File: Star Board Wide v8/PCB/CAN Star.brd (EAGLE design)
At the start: 124.7 x 37.3 mm, 24 parts

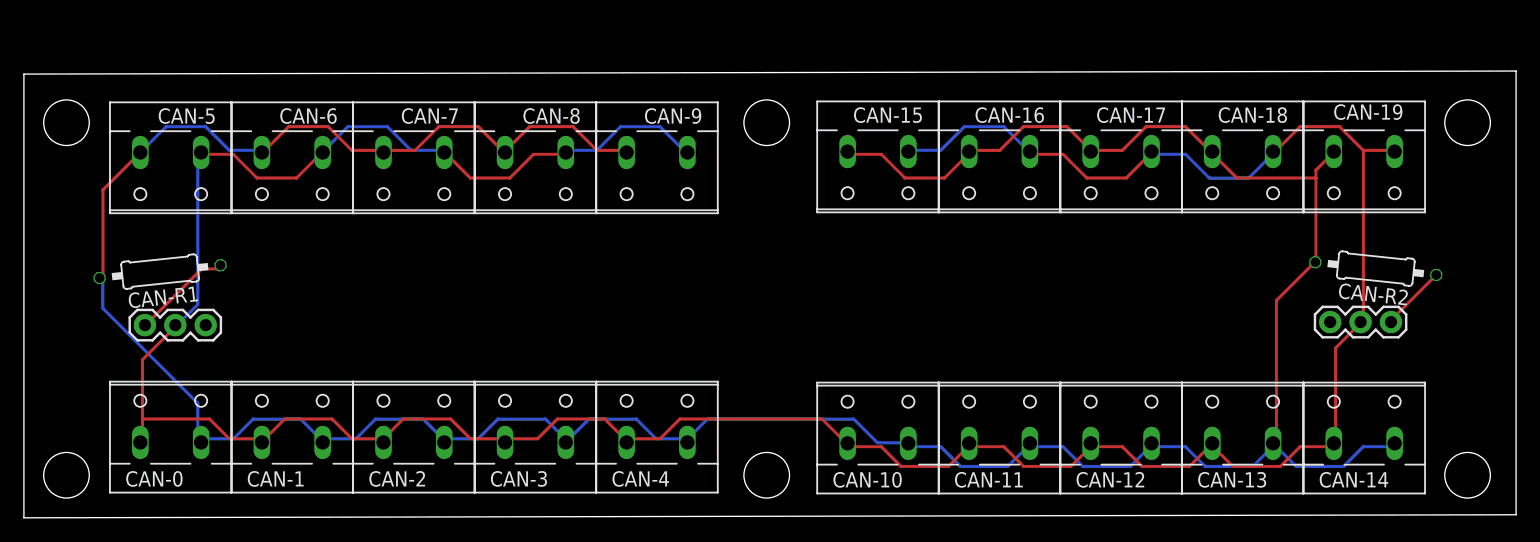
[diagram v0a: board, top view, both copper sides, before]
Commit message: switch to wide-v9, add in grounds, removed odd connections, needs layout work
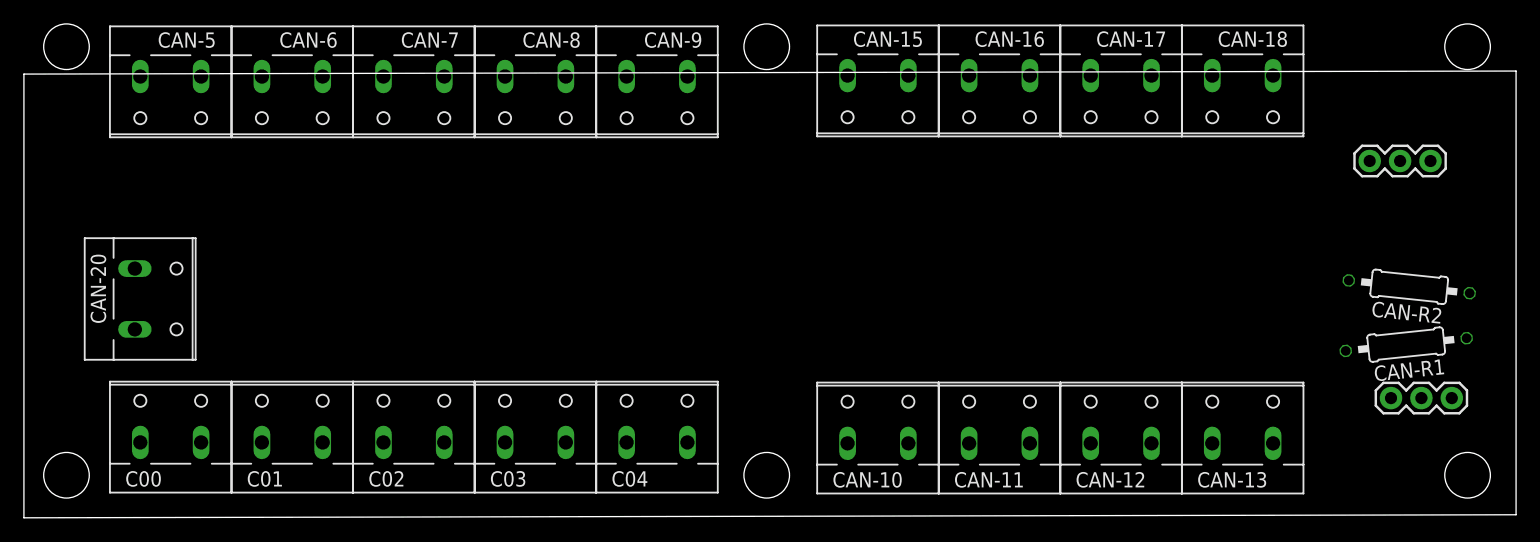
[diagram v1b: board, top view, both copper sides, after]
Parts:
- removed CAN-14: CAN 4, con-wago-508:W237-132
- removed CAN-19: CAN 9, con-wago-508:W237-132
- added CAN-20: CAN GND, con-wago-508:W237-132
- C00: value CAN 0 -> (none)
- moved CAN-R1 104.3 mm to (115.5, 14.5)
- moved JUMPER1 104.3 mm to (114.3, 10.0)
- moved JUMPER2 13.9 mm to (117.5, 29.8)
- moved CAN-15 6.35 mm to (71.4, 36.3)
- moved CAN-16 6.35 mm to (81.5, 36.3)
- moved CAN-17 6.35 mm to (91.7, 36.3)
- moved CAN-18 6.35 mm to (101.9, 36.3)
- moved CAN-5 6.35 mm to (12.3, 36.2)
- moved CAN-6 6.35 mm to (22.4, 36.2)
- moved CAN-7 6.35 mm to (32.6, 36.2)
- moved CAN-8 6.35 mm to (42.7, 36.2)
- moved CAN-9 6.35 mm to (52.9, 36.2)
- moved CAN-R2 3.18 mm to (115.8, 19.3)
- renumbered CAN-0 to C00, CAN-1 to C01, CAN-2 to C02, CAN-3 to C03, CAN-4 to C04
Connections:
- removed net CAN-A: C00.1, C01.1, C02.1, C03.1, C04.1, CAN-10.1, CAN-11.1, CAN-12.1, CAN-13.1, CAN-14.1, CAN-15.1, CAN-16.1, CAN-17.1, CAN-18.1, CAN-19.1, CAN-5.1, CAN-6.1, CAN-7.1, CAN-8.1, CAN-9.1, JUMPER1.2, JUMPER2.2
- removed net CAN-B: C00.2, C01.2, C02.2, C03.2, C04.2, CAN-10.2, CAN-11.2, CAN-12.2, CAN-13.2, CAN-14.2, CAN-15.2, CAN-16.2, CAN-17.2, CAN-18.2, CAN-19.2, CAN-5.2, CAN-6.2, CAN-7.2, CAN-8.2, CAN-9.2, CAN-R1.2, CAN-R2.2
- new net G: C00.2, C02.1, C03.2, CAN-10.1, CAN-11.2, CAN-13.1, CAN-15.2, CAN-16.1, CAN-18.2, CAN-5.1, CAN-7.2, CAN-8.1, CAN-R1.2, CAN-R2.2
- new net GND: C01.1, C02.2, C04.1, CAN-10.2, CAN-12.1, CAN-13.2, CAN-15.1, CAN-17.2, CAN-18.1, CAN-20.1, CAN-20.2, CAN-6.2, CAN-7.1, CAN-9.2
- new net Y: C00.1, C01.2, C03.1, C04.2, CAN-11.1, CAN-12.2, CAN-16.2, CAN-17.1, CAN-5.2, CAN-6.1, CAN-8.2, CAN-9.1, JUMPER1.2, JUMPER2.2
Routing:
- net CAN-B: track 264.5 -> 0.00 mm
- net CAN-A: track 261.7 -> 0.00 mm
- net N$1: track 8.40 -> 0.54 mm
- net N$2: track 5.50 -> 0.22 mm
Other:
- board text added: "GND"
- board text added: "Star Board Wide v9"
- board text removed: "Star Board Wide v8"

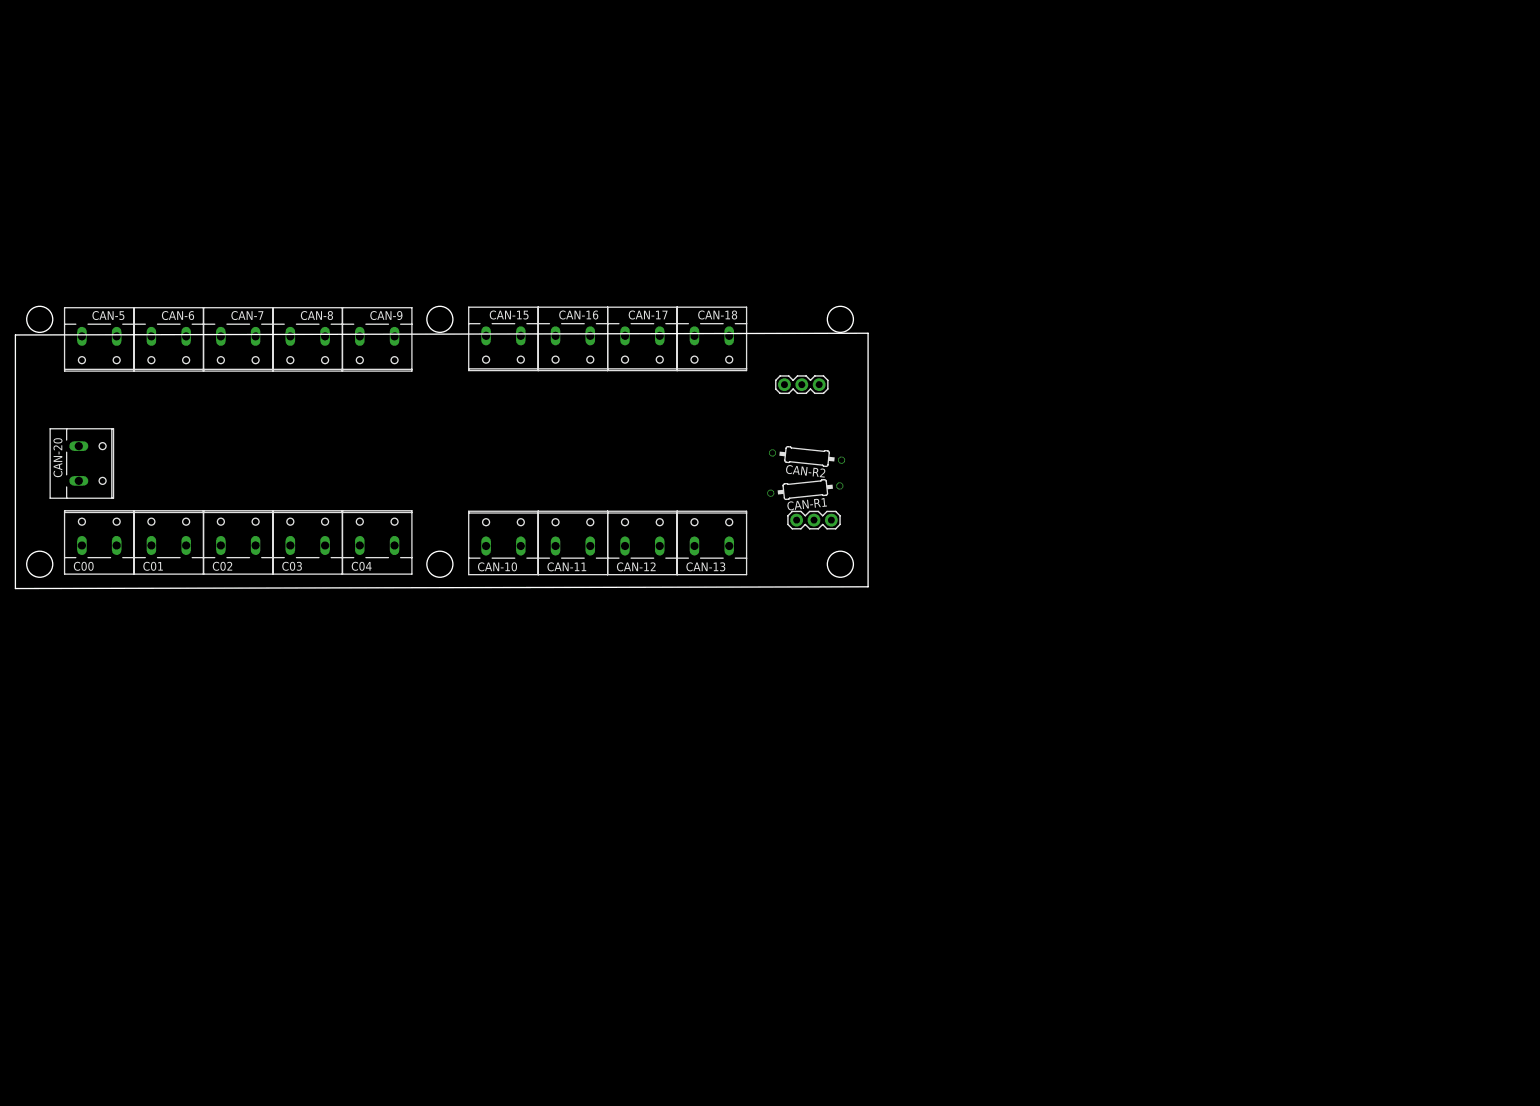
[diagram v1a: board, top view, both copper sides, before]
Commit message: change layout to 3 by 4
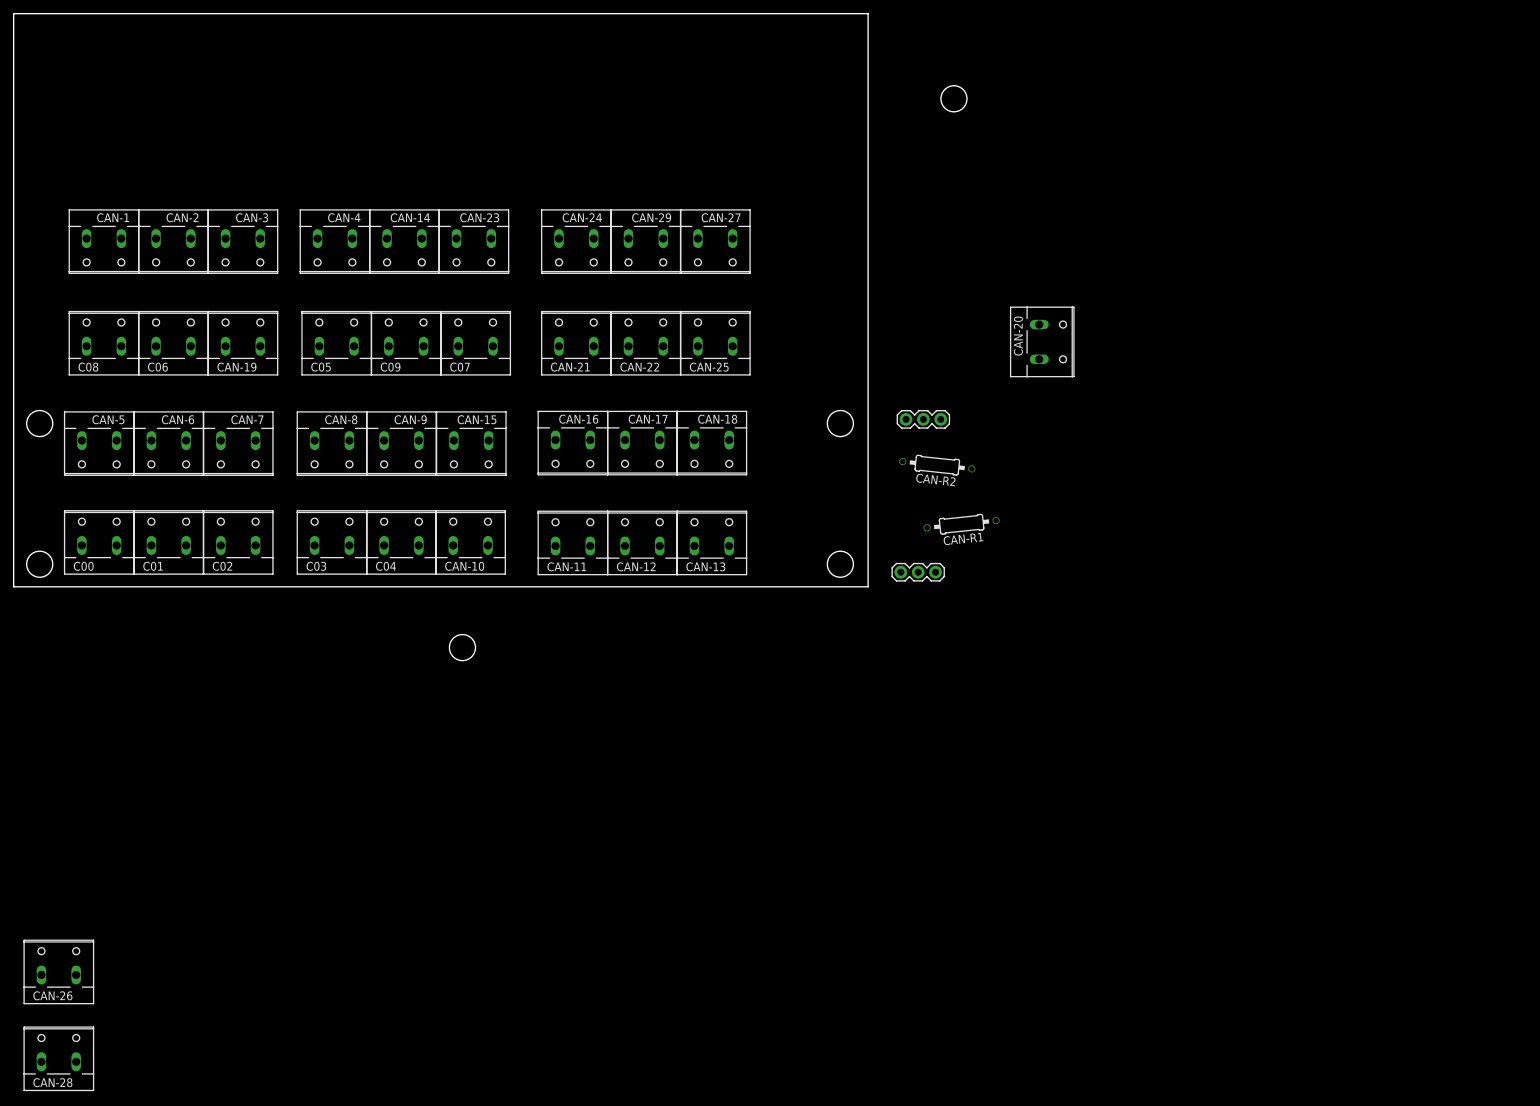
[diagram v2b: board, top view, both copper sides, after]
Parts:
- added C05: (no value), con-wago-508:W237-132
- added C06, CAN-21, CAN-26: CAN 1, con-wago-508:W237-132
- added C07, CAN-22, CAN-27: CAN 2, con-wago-508:W237-132
- added C08: CAN 3, con-wago-508:W237-132
- added C09: CAN 4, con-wago-508:W237-132
- added CAN-1, CAN-23: CAN 5, con-wago-508:W237-132
- added CAN-14: CAN 9, con-wago-508:W237-132
- added CAN-19: CAN 0, con-wago-508:W237-132
- added CAN-2, CAN-24, CAN-28: CAN 6, con-wago-508:W237-132
- added CAN-25, CAN-29, CAN-3: CAN 7, con-wago-508:W237-132
- added CAN-4: CAN 8, con-wago-508:W237-132
- moved CAN-20 141.6 mm to (150.4, 36.1)
- moved CAN-R1 23.4 mm to (138.4, 9.40)
- moved CAN-R2 19.1 mm to (134.8, 18.0)
- moved JUMPER2 18.5 mm to (135.3, 24.7)
- moved JUMPER1 17.0 mm to (129.5, 2.39)
- moved CAN-15 16.0 mm to (66.7, 21.0)
- moved CAN-8 15.6 mm to (46.3, 21.0)
- moved CAN-9 15.6 mm to (56.5, 21.0)
- moved CAN-16 15.2 mm to (81.5, 21.1)
- moved CAN-17 15.2 mm to (91.7, 21.1)
- moved CAN-18 15.2 mm to (101.9, 21.1)
- moved CAN-5 15.2 mm to (12.3, 21.0)
- moved CAN-6 15.2 mm to (22.4, 21.0)
- moved CAN-7 15.2 mm to (32.6, 21.0)
- moved CAN-10 4.80 mm to (66.6, 6.93)
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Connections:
- net G: now also C05.2, C07.1, C08.2, CAN-1.1, CAN-19.1, CAN-21.2, CAN-23.2, CAN-24.1, CAN-25.1, CAN-26.2, CAN-27.2, CAN-28.1, CAN-3.2, CAN-4.1
- net GND: now also C06.1, C07.2, C09.1, CAN-14.2, CAN-19.2, CAN-2.2, CAN-22.1, CAN-23.1, CAN-25.2, CAN-27.1, CAN-29.2, CAN-3.1
- net Y: now also C05.1, C06.2, C08.1, C09.2, CAN-1.2, CAN-14.1, CAN-2.1, CAN-21.1, CAN-22.2, CAN-24.2, CAN-26.1, CAN-28.2, CAN-29.1, CAN-4.2
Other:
- board size 124.7 x 37.3 mm -> 125 x 83.8 mm

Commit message: Remade board wide v9
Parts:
- removed C00, C05: (no value), con-wago-508:W237-132
- removed C01, C06, CAN-11, CAN-21, CAN-26: CAN 1, con-wago-508:W237-132
- removed C02, C07, CAN-12, CAN-22, CAN-27: CAN 2, con-wago-508:W237-132
- removed C03, C08, CAN-13: CAN 3, con-wago-508:W237-132
- removed C04, C09: CAN 4, con-wago-508:W237-132
- removed CAN-1, CAN-15, CAN-23, CAN-5: CAN 5, con-wago-508:W237-132
- removed CAN-10, CAN-19: CAN 0, con-wago-508:W237-132
- removed CAN-14, CAN-9: CAN 9, con-wago-508:W237-132
- removed CAN-16, CAN-2, CAN-24, CAN-28, CAN-6: CAN 6, con-wago-508:W237-132
- removed CAN-17, CAN-25, CAN-29, CAN-3, CAN-7: CAN 7, con-wago-508:W237-132
- removed CAN-18, CAN-4, CAN-8: CAN 8, con-wago-508:W237-132
- removed CAN-20: CAN GND, con-wago-508:W237-132
- removed CAN-R1, CAN-R2: 120Ω, resistor:0207/10
- removed JUMPER1, JUMPER2: (no value), SparkFun-Connectors:1X03
- added U$1, U$10, U$11, U$12, U$2, U$3, U$4, U$5, U$6, U$7, U$8, U$9: 2-3-TERMS, custom:GREEN-2-TERMS
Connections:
- removed net G: C00.2, C02.1, C03.2, C05.2, C07.1, C08.2, CAN-1.1, CAN-10.1, CAN-11.2, CAN-13.1, CAN-15.2, CAN-16.1, CAN-18.2, CAN-19.1, CAN-21.2, CAN-23.2, CAN-24.1, CAN-25.1, CAN-26.2, CAN-27.2, CAN-28.1, CAN-3.2, CAN-4.1, CAN-5.1, CAN-7.2, CAN-8.1, CAN-R1.2, CAN-R2.2
- removed net N$1: CAN-R1.1, JUMPER1.1
- removed net N$2: CAN-R2.1, JUMPER2.1
- removed net Y: C00.1, C01.2, C03.1, C04.2, C05.1, C06.2, C08.1, C09.2, CAN-1.2, CAN-11.1, CAN-12.2, CAN-14.1, CAN-16.2, CAN-17.1, CAN-2.1, CAN-21.1, CAN-22.2, CAN-24.2, CAN-26.1, CAN-28.2, CAN-29.1, CAN-4.2, CAN-5.2, CAN-6.1, CAN-8.2, CAN-9.1, JUMPER1.2, JUMPER2.2
- new net G(L): U$1.L0, U$1.L1, U$10.L0, U$10.L1, U$11.L0, U$11.L1, U$12.L0, U$12.L1, U$2.L0, U$2.L1, U$3.L0, U$3.L1, U$4.L0, U$4.L1, U$5.L0, U$5.L1, U$6.L0, U$6.L1, U$7.L0, U$7.L1, U$8.L0, U$8.L1, U$9.L0, U$9.L1
- new net Y(H): U$1.H0, U$1.H1, U$10.H0, U$10.H1, U$11.H0, U$11.H1, U$12.H0, U$12.H1, U$2.H0, U$2.H1, U$3.H0, U$3.H1, U$4.H0, U$4.H1, U$5.H0, U$5.H1, U$6.H0, U$6.H1, U$7.H0, U$7.H1, U$8.H0, U$8.H1, U$9.H0, U$9.H1
- net GND: now also U$1.GND0, U$1.GND1, U$10.GND0, U$10.GND1, U$11.GND0, U$11.GND1, U$12.GND0, U$12.GND1, U$2.GND0, U$2.GND1, U$3.GND0, U$3.GND1, U$4.GND0, U$4.GND1, U$5.GND0, U$5.GND1, U$6.GND0, U$6.GND1, U$7.GND0, U$7.GND1, U$8.GND0, U$8.GND1, U$9.GND0, U$9.GND1; no longer C01.1, C02.2, C04.1, C06.1, C07.2, C09.1, CAN-10.2, CAN-12.1, CAN-13.2, CAN-14.2, CAN-15.1, CAN-17.2, CAN-18.1, CAN-19.2, CAN-2.2, CAN-20.1, CAN-20.2, CAN-22.1, CAN-23.1, CAN-25.2, CAN-27.1, CAN-29.2, CAN-3.1, CAN-6.2, CAN-7.1, CAN-9.2
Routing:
- net N$1: track 0.54 -> 0.00 mm
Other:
- board size 125 x 83.8 mm -> 221 x 38.1 mm
- board text added: "RoboLoCo | Team 5338"
- board text removed: "G(L)"
- board text removed: "GND"
- board text removed: "ON"
- board text removed: "RoboLoCo Team 5338"
- board text removed: "Y(H)"

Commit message: Auto routed
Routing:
- net GND: track 0.00 -> 419.7 mm
- net G(L): track 0.00 -> 385.3 mm
- net Y(H): track 0.00 -> 377.8 mm

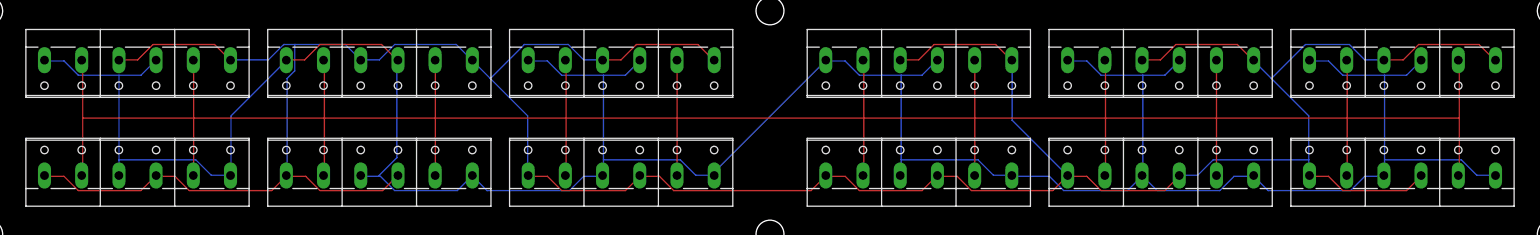
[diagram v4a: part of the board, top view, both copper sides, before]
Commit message: Rerouted with better nets for gnd
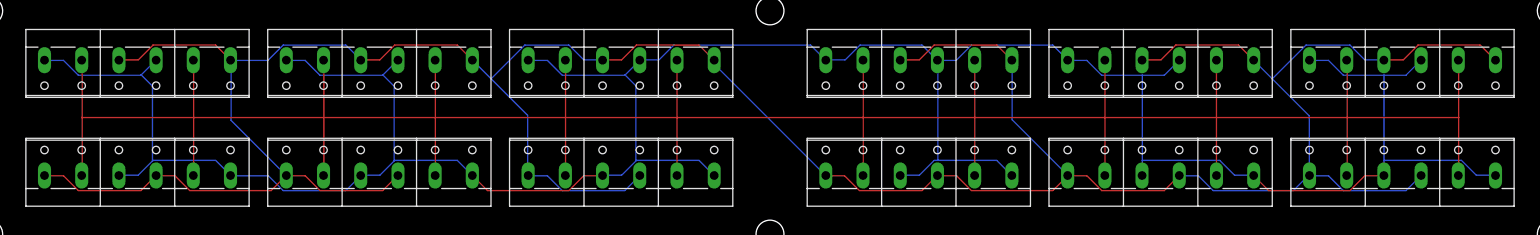
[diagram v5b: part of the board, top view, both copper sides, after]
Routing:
- net GND: track 419.7 -> 415.2 mm
- net Y(H): track 377.8 -> 377.3 mm
